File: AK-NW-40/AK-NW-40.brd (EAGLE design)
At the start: 120 x 110 mm, 4 parts, among them J1 POWER_JACK-SLOTS

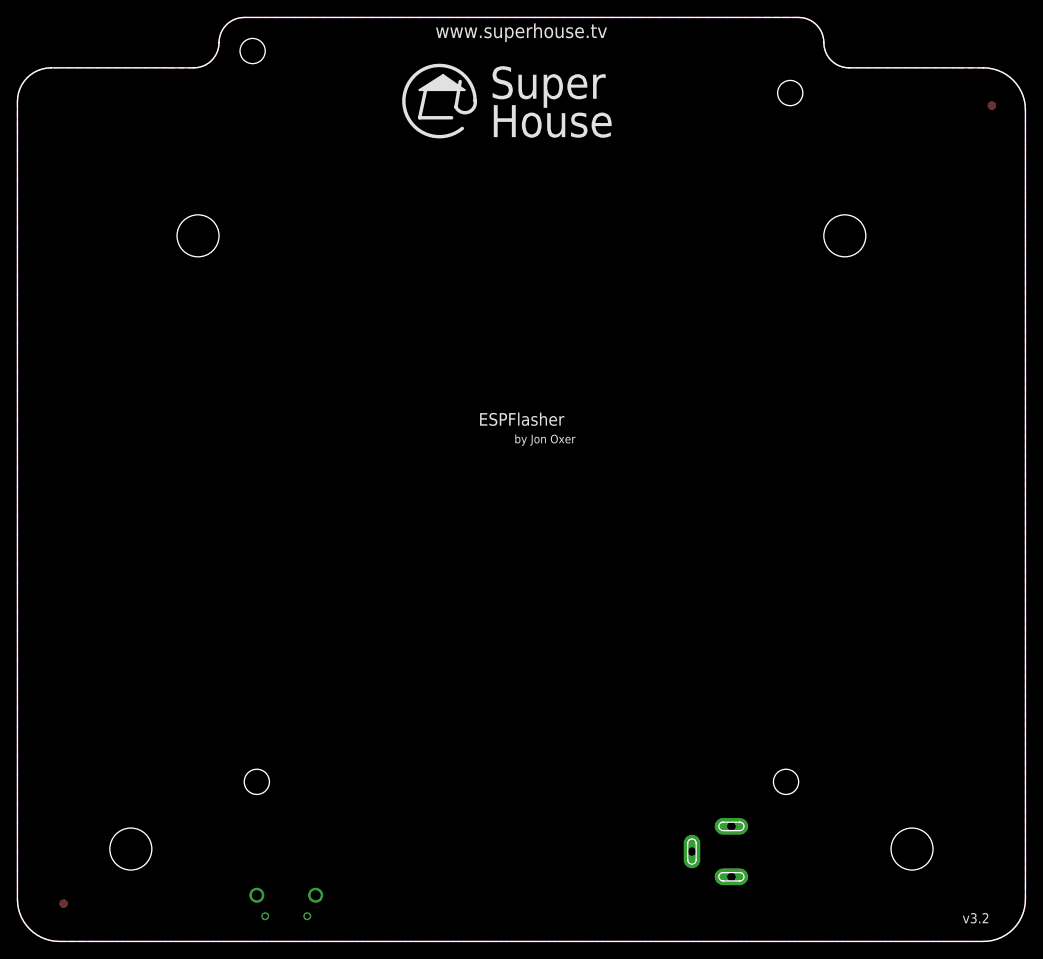
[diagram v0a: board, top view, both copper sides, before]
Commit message: Fixed hole positions based on drawings provided by SZOMK.
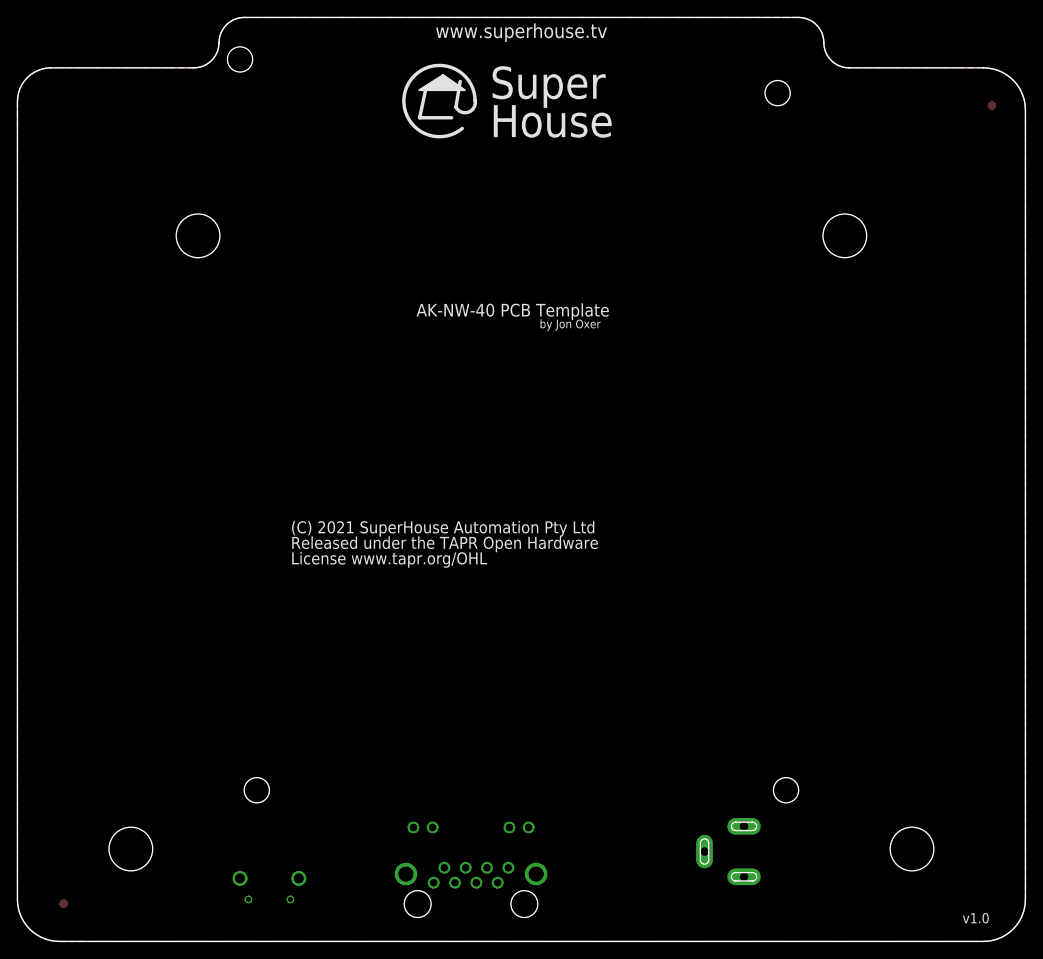
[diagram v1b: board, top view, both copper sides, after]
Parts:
- added U$3: RJHSE538X-INVERTED, SuperHouse-Connectors:RJHSE538X
- moved U$2 2.83 mm to (-30.0, 5.00)
- moved J1 1.50 mm to (26.5, 0.00)
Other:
- board text added: "(C) 2021 SuperHouse Automation Pty Ltd Released under the TAPR Open Hardware License www.tapr.org/OHL"
- board text added: "AK-NW-40 PCB Template"
- board text added: "v1.0"
- board text removed: "(C) 2019-2021 SuperHouse Automation Released under the TAPR Open Hardware License www.tapr.org/OHL"
- board text removed: "ESPFlasher"
- board text removed: "v3.2"
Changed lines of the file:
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@@
 <plain>
 <text x="0" y="107.55" size="1.6764" layer="21" font="vector" ratio="18" align="bottom-center">www.superhouse.tv</text>
-<text x="52.5" y="2.1636" size="1.2" layer="21" font="vector" ratio="15">v3.2</text>
-<text x="0" y="61.4" size="1.5" layer="21" font="vector" ratio="18" align="bottom-center">ESPFlasher</text>
-<text x="2.8" y="59.3" size="1.016" layer="21" font="vector" ratio="17" align="bottom-center">by Jon Oxer</text>
-<text x="-16.54" y="14.11" size="0.88" layer="22" font="vector" ratio="16" distance="30" rot="MR180">(C) 2019-2021 SuperHouse Automation
+<text x="52.5" y="2.1636" size="1.2" layer="21" font="vector" ratio="15">v1.0</text>
+<text x="-1" y="74.4" size="1.5" layer="21" font="vector" ratio="18" align="bottom-center">AK-NW-40 PCB Template</text>
+<text x="5.8" y="73" size="1.016" layer="21" font="vector" ratio="17" align="bottom-center">by Jon Oxer</text>
+<text x="-27.46" y="44.89" size="1.4224" layer="21" font="vector" ratio="16" distance="30">(C) 2021 SuperHouse Automation Pty Ltd
 Released under the TAPR Open Hardware
 License www.tapr.org/OHL</text>
@@
 <text x="25.65" y="15.25" size="0.6096" layer="27">K</text>
 <text x="25.65" y="17.75" size="0.6096" layer="27">K</text>
-<hole x="46.5" y="11" drill="5"/>
-<hole x="-46.5" y="11" drill="5"/>
-<hole x="-38.5" y="84" drill="5"/>
-<hole x="38.5" y="84" drill="5"/>
-<hole x="-31.5" y="19" drill="3"/>
-<hole x="31.5" y="19" drill="3"/>
-<hole x="-32" y="106" drill="3"/>
-<hole x="32" y="101" drill="3"/>
+<hole x="46.5" y="11" drill="5.2" locked="yes"/>
+<hole x="-46.5" y="11" drill="5.2" locked="yes"/>
+<hole x="-38.5" y="84" drill="5.2" locked="yes"/>
+<hole x="38.5" y="84" drill="5.2" locked="yes"/>
+<hole x="-31.5" y="18" drill="3" locked="yes"/>
+<hole x="31.5" y="18" drill="3" locked="yes"/>
+<hole x="-33.5" y="105" drill="3" locked="yes"/>
+<hole x="30.5" y="100.99" drill="3" locked="yes"/>
 <wire x1="-55" y1="0" x2="55" y2="0" width="0.1524" layer="20"/>
 <wire x1="-55" y1="0" x2="-60" y2="5" width="0.1524" layer="20" curve="-90"/>
@@
 <wire x1="36" y1="107" x2="39" y2="104" width="0.1524" layer="20" curve="90"/>
 <wire x1="-36" y1="107" x2="-39" y2="104" width="0.1524" layer="20" curve="-90"/>
-<wire x1="-38.5" y1="89" x2="-38.5" y2="79" width="1.016" layer="52"/>
-<wire x1="38.5" y1="89" x2="38.5" y2="79" width="1.016" layer="52"/>
-<wire x1="46.5" y1="16" x2="46.5" y2="6" width="1.016" layer="52"/>
-<wire x1="-46.5" y1="16" x2="-46.5" y2="6" width="1.016" layer="52"/>
+<wire x1="-38.5" y1="89" x2="-38.5" y2="79" width="1.016" layer="52" locked="yes"/>
+<wire x1="38.5" y1="89" x2="38.5" y2="79" width="1.016" layer="52" locked="yes"/>
+<wire x1="46.5" y1="16" x2="46.5" y2="6" width="1.016" layer="52" locked="yes"/>
+<wire x1="-46.5" y1="16" x2="-46.5" y2="6" width="1.016" layer="52" locked="yes"/>
 </plain>
 <attributes>
@@
 <element name="FID1" library="SuperHouse-Symbols" library_urn="urn:adsk.eagle:library:13228893" package="FIDUCIAL-1X2.5" package3d_urn="urn:adsk.eagle:package:13228898/2" value="FIDUCIAL1X2.5" x="-54.5" y="4.5" smashed="yes"/>
 <element name="FID2" library="SuperHouse-Symbols" library_urn="urn:adsk.eagle:library:13228893" package="FIDUCIAL-1X2.5" package3d_urn="urn:adsk.eagle:package:13228898/2" value="FIDUCIAL1X2.5" x="56" y="99.5" smashed="yes"/>
-<element name="J1" library="SuperHouse-Connectors" library_urn="urn:adsk.eagle:library:11765989" package="POWER_JACK_SLOTS" package3d_urn="urn:adsk.eagle:package:7066536/4" value="POWER_JACK-SLOTS" x="25" y="0" smashed="yes" rot="MR0">
-<attribute name="NAME" x="28.81" y="5.08" size="0.4064" layer="26" rot="MR0"/>
-<attribute name="VALUE" x="28.81" y="3.81" size="0.4064" layer="28" rot="MR0"/>
+<element name="J1" library="SuperHouse-Connectors" library_urn="urn:adsk.eagle:library:11765989" package="POWER_JACK_SLOTS" package3d_urn="urn:adsk.eagle:package:7066536/4" value="POWER_JACK-SLOTS" x="26.5" y="0" smashed="yes" rot="MR0">
+<attribute name="NAME" x="30.31" y="5.08" size="0.4064" layer="26" rot="MR0"/>
+<attribute name="VALUE" x="30.31" y="3.81" size="0.4064" layer="28" rot="MR0"/>
 </element>
-<element name="U$2" library="SuperHouse-Switches" library_urn="urn:adsk.eagle:library:11744182" package="TC-120V" package3d_urn="urn:adsk.eagle:package:11818000/1" value="TAC-SWITCH-2PIN-GND-FSMMSHPTR" x="-28" y="3" smashed="yes" rot="MR180">
-<attribute name="NAME" x="-32" y="-1" size="1.778" layer="26" rot="MR180"/>
-<attribute name="VALUE" x="-32" y="9" size="1.778" layer="28" rot="MR180"/>
+<element name="U$2" library="SuperHouse-Switches" library_urn="urn:adsk.eagle:library:11744182" package="TC-120V" package3d_urn="urn:adsk.eagle:package:11818000/1" value="TAC-SWITCH-2PIN-GND-FSMMSHPTR" x="-30" y="5" smashed="yes" rot="MR180">
+<attribute name="NAME" x="-34" y="1" size="1.778" layer="26" rot="MR180"/>
+<attribute name="VALUE" x="-34" y="11" size="1.778" layer="28" rot="MR180"/>
+</element>
+<element name="U$3" library="SuperHouse-Connectors" library_urn="urn:adsk.eagle:library:11765989" package="RJHSE538X" package3d_urn="urn:adsk.eagle:package:30747766/3" value="RJHSE538X-INVERTED" x="-6" y="-1" smashed="yes" rot="MR0">
+<attribute name="NAME" x="-4.46" y="2.35" size="0.8128" layer="26" rot="MR0"/>
+<attribute name="VALUE" x="-4.46" y="1.08" size="0.8128" layer="28" rot="MR0"/>
 </element>
 </elements>
@@
 </polygon>
 <polygon width="0.1524" layer="16">
-<vertex x="-20" y="110"/>
 <vertex x="-33" y="110" curve="90"/>
 <vertex x="-36" y="107" curve="-90"/>
@@
 packages will not be understood (or retained) with this version.
 </note>
+<note version="8.5" severity="warning">
+Since Version 8.5, EAGLE supports locking for holes, vias, wires and polygons.
+The locking property on all objects of these types will not be understood in this version.
+</note>
 </compatibility>
